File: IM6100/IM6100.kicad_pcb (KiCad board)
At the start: 4 copper layers, 180 x 120 mm, 125 parts, among them SW1 SS-12SDP2, SW10 SS-12SDP2, SW11 SS-12SDP2, SW12 SS-12SDP2, SW13 DTSM-644R-V-T/R, SW14 SS-12SDP2, SW15 DTSM-644R-V-T/R, SW16 DTSM-644R-V-T/R, SW17 SS-12SDP2, SW18 DTSM-644R-V-T/R, SW19 ERD216CSZ, SW2 SS-12SDP2, SW20 DTSM-644R-V-T/R, SW3 SS-12SDP2, SW4 SS-12SDP2, SW5 SS-12SDP2, SW6 SS-12SDP2, SW7 SS-12SDP2, SW8 SS-12SDP2, SW9 SS-12SDP2, U1 IM6100, U10 SN74LVC245APW, U11 SN74LVC574APW, U12 SN74LVC574APW, U2 TXB0108PW, U3 TXB0108PW, U4 TXB0108PW, U5 TXB0108PW, U6 Tang_Nano_9K, U7 SN74LVC574APW, U8 SN74LVC245APW, U9 SN74LVC574APW, Y1 4MHz

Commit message: Removed Pull-dow on ~RESET.
TXB0108 can't use pull-up and -down.
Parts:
- removed R2: 51K, 0my_project:R_1608_0603
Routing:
- net GND: track 713.1 -> 692.4 mm, vias 101 -> 102
- net /~{RESET_3V3}: track 144.8 -> 141.2 mm
- net /SINGLE_SW: track 57.2 -> 58.3 mm
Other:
- board text added: "S1/2: Reset"

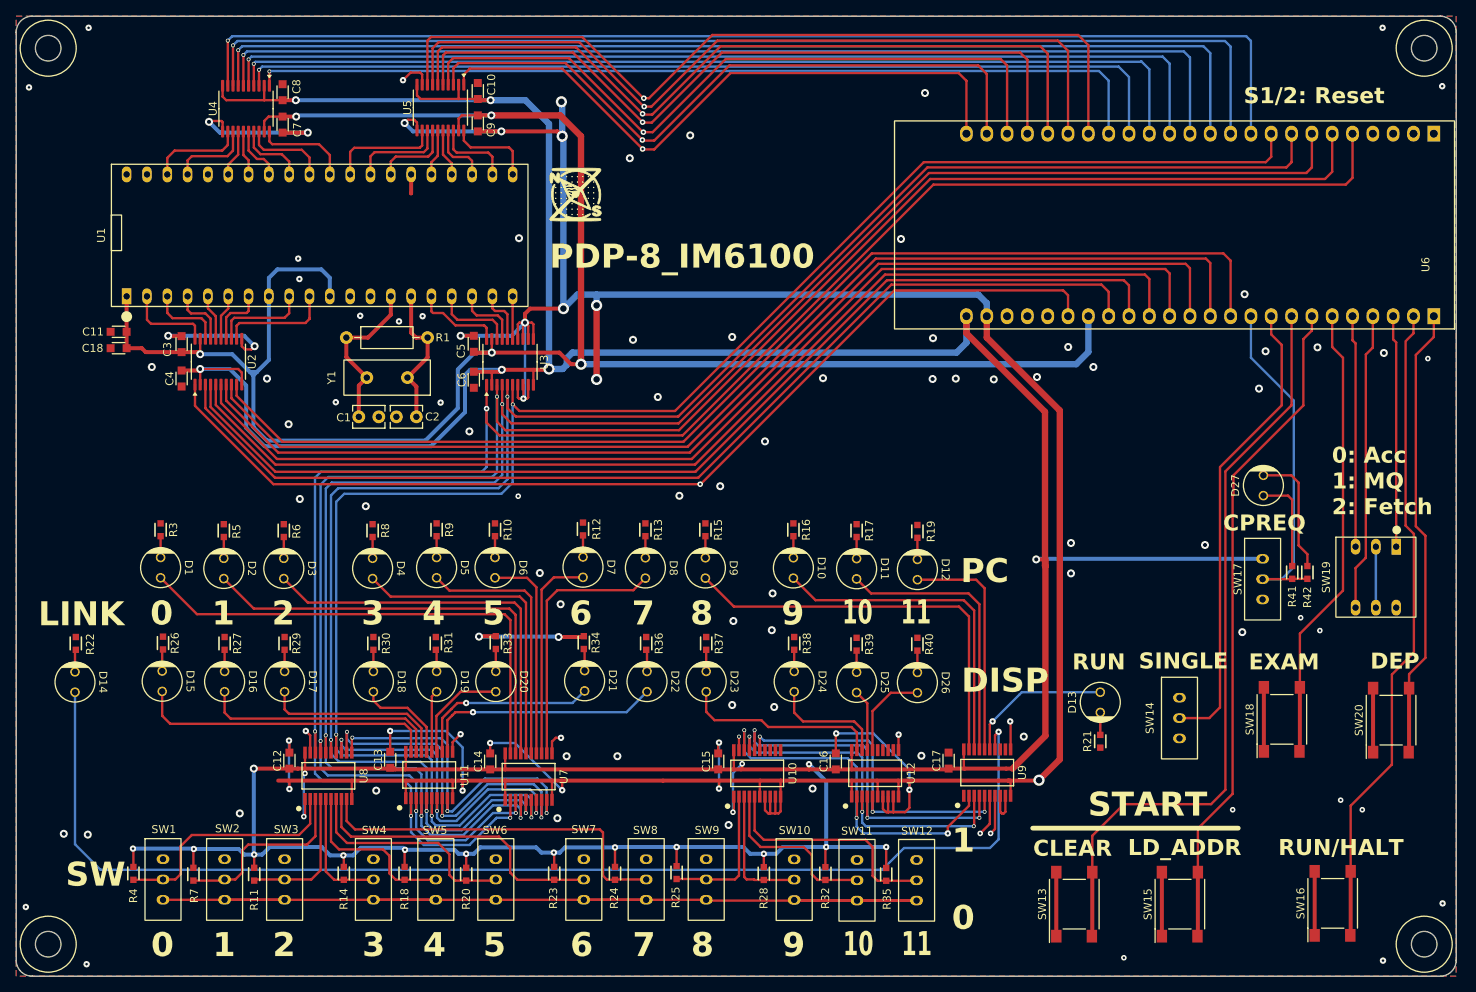
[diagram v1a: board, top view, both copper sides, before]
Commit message: Fixed to reset IM6100 during setting up Tang Nano 9K.
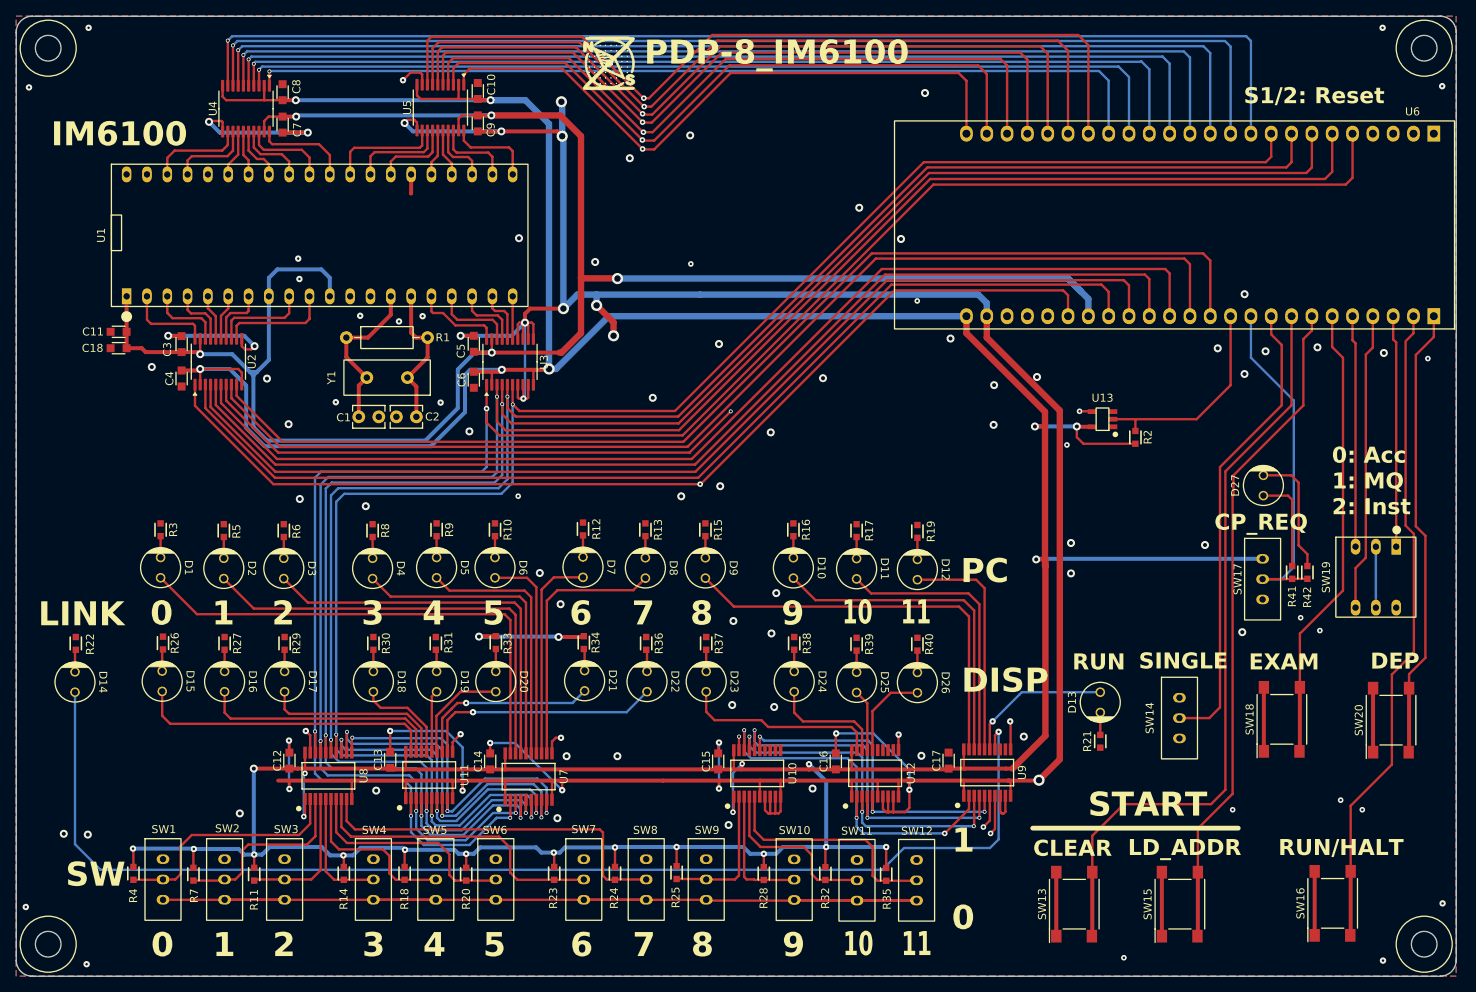
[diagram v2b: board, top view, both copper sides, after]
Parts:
- added R2: 10K, 0my_project:R_1608_0603, F.Cu at (186.0, 83.3)
- added U13: SN74AHC1G04, 0my_project:SOT-23-5_TI, F.Cu at (181.9, 81.1)
- moved IMG1 16.9 mm to (120.2, 36.6)
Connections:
- U6 pad 36: /~{RESET_3V3} -> /XTA_3V3
- U6 pad 37: /XTA_3V3 -> /LXMAR_3V3
- U6 pad 38: /LXMAR_3V3 -> MK_RESET
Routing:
- net MK_RESET: track 0.00 -> 26.6 mm
- net /~{RESET_3V3}: track 141.2 -> 115.1 mm, vias 0 -> 2
- net +3.3V: track 586.2 -> 601.2 mm, vias 24 -> 26
- net /LINK_3V3: track 173.6 -> 169.6 mm
- net +5V: track 255.5 -> 252.5 mm
- net GND: track 692.4 -> 689.7 mm, vias 102 -> 104
- net /XTA_3V3: track 143.2 -> 140.6 mm
- net /LXMAR_3V3: track 145.1 -> 142.6 mm
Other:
- board text added: "0: Acc 1: MQ 2: Inst"
- board text added: "CP_REQ"
- board text added: "DRC Error: 2, warning: 28"
- board text added: "IM6100"
- board text removed: "0: Acc 1: MQ 2: Fetch"
- board text removed: "CPREQ"
- board text removed: "DRC Error: 2, warning: 27"

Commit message: Updated tactile switch.
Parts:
- SW13, SW15, SW16, SW18, SW20: value DTSM-644R-V-T/R -> DTSM-63N-V-T/R
